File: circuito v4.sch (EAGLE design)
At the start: 64 parts, among them IC1 LM324N

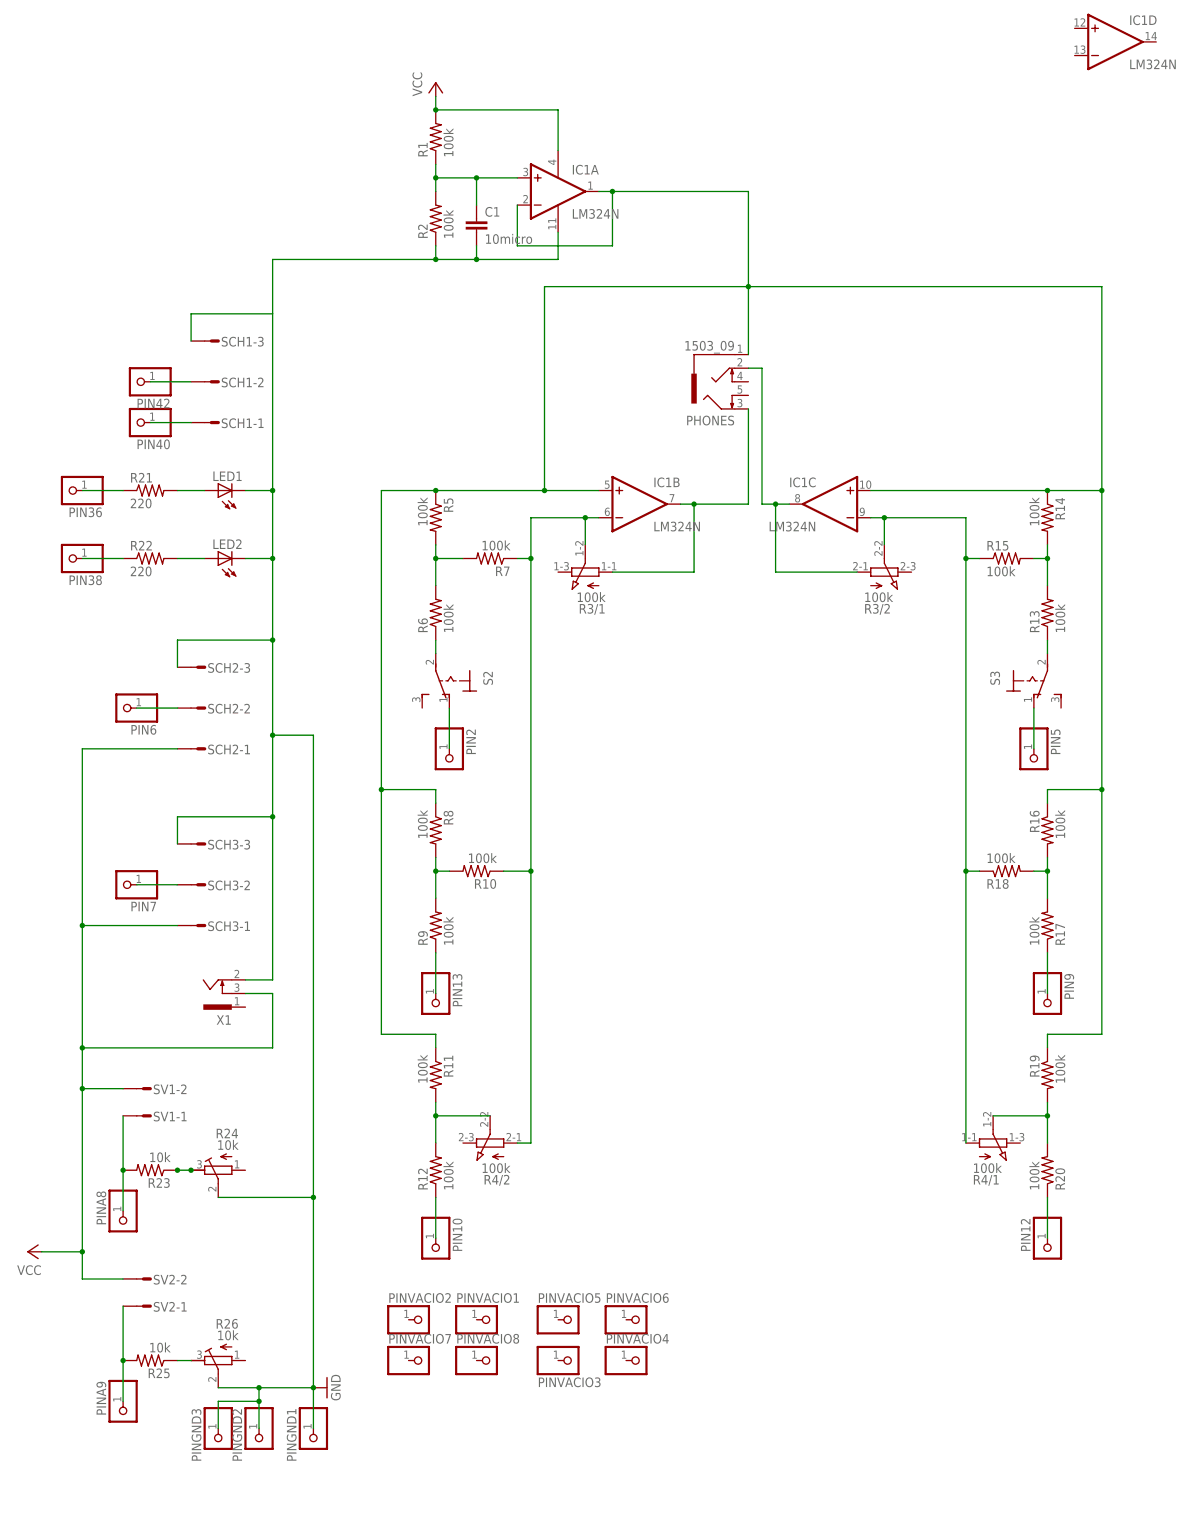
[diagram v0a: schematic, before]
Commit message: Agregado de recuadros con texto
Muestran que es cada parte delcircuito
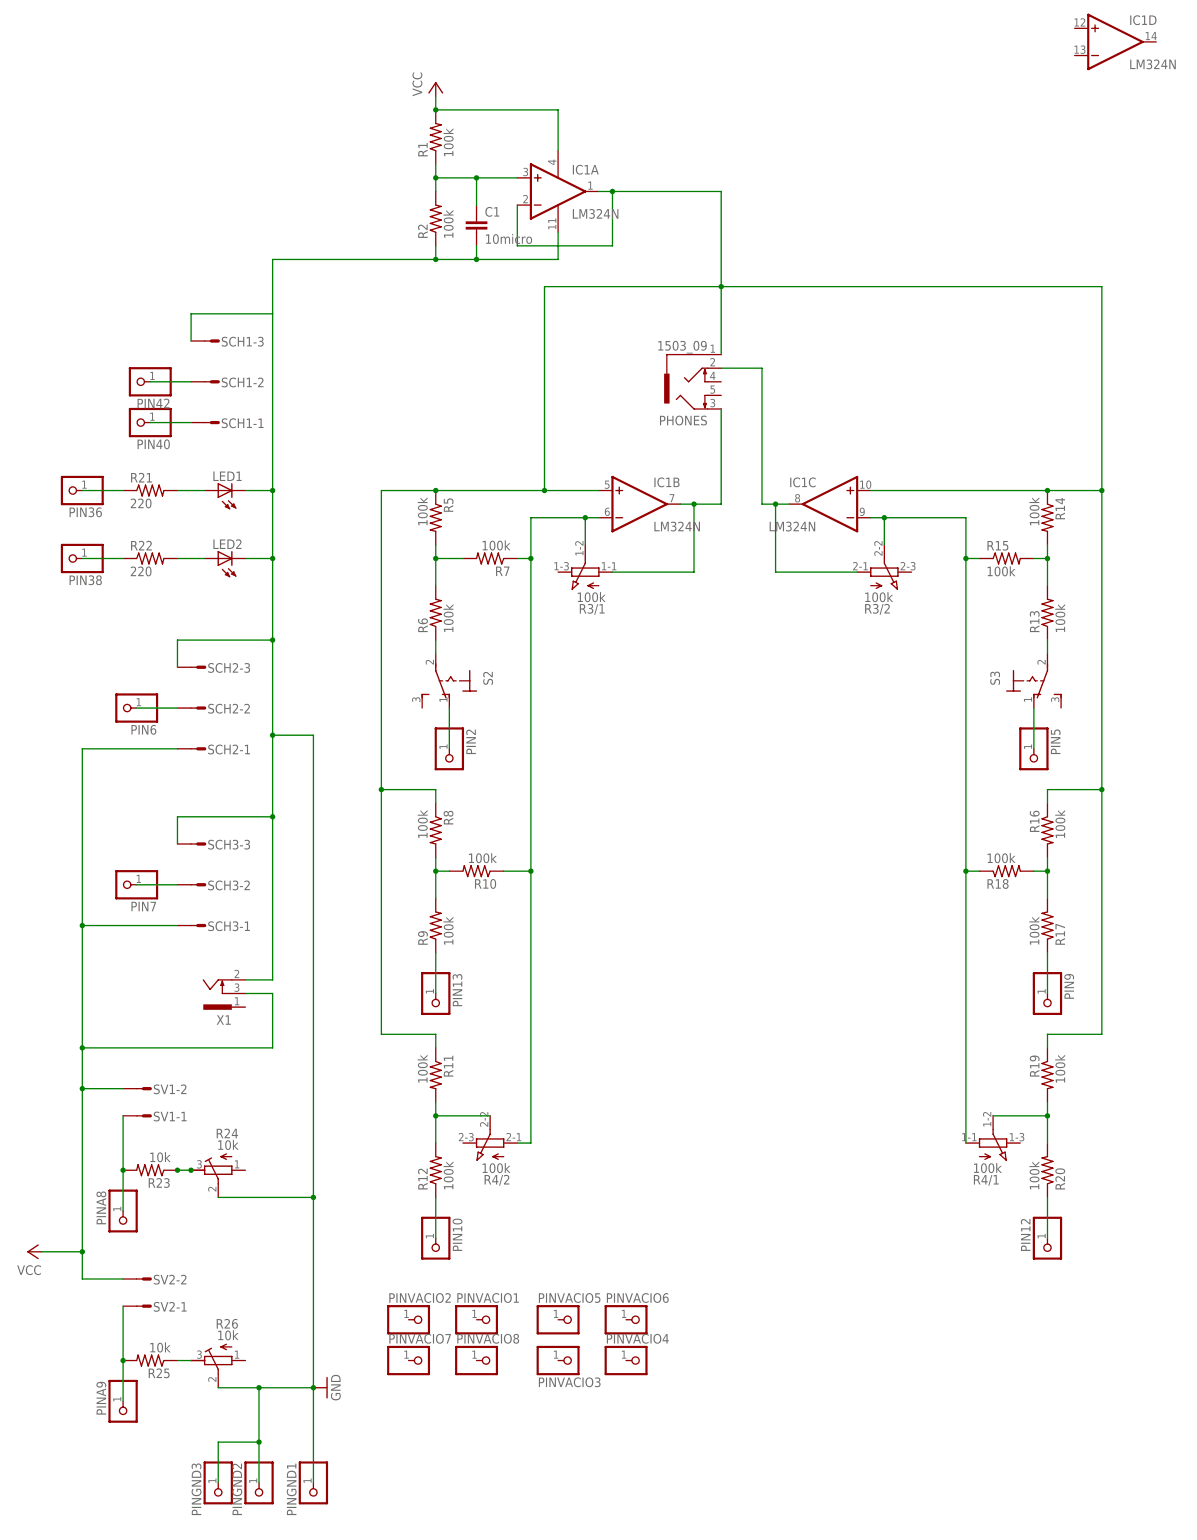
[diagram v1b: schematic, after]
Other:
- note added: "Conexion Servos"
- note added: "FSR (izq y der)"
- note added: "LEDs y sincronizacion"
- note added: "Rama derecha de audio"
- note added: "Rama izquierda del audio"
- note added: "Tierra virtual"
- moved on the sheet: PHONES, PINGND1, PINGND2, PINGND3
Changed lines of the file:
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@@
 <sheet>
 <plain>
+<wire x1="-27.94" y1="106.68" x2="-27.94" y2="63.5" width="0.1524" layer="150"/>
+<wire x1="-27.94" y1="63.5" x2="22.86" y2="63.5" width="0.1524" layer="150"/>
+<wire x1="22.86" y1="63.5" x2="22.86" y2="106.68" width="0.1524" layer="150"/>
+<wire x1="22.86" y1="106.68" x2="-27.94" y2="106.68" width="0.1524" layer="150"/>
+<text x="-10.16" y="109.22" size="1.778" layer="150">Tierra virtual</text>
+<wire x1="-30.48" y1="30.48" x2="35.56" y2="30.48" width="0.1524" layer="150"/>
+<wire x1="35.56" y1="30.48" x2="35.56" y2="-121.92" width="0.1524" layer="150"/>
+<wire x1="35.56" y1="-121.92" x2="-30.48" y2="-121.92" width="0.1524" layer="150"/>
+<wire x1="-30.48" y1="-121.92" x2="-30.48" y2="30.48" width="0.1524" layer="150"/>
+<text x="-22.86" y="33.02" size="1.778" layer="150">Rama derecha de audio</text>
+<wire x1="43.18" y1="30.48" x2="43.18" y2="-121.92" width="0.1524" layer="150"/>
+<wire x1="43.18" y1="-121.92" x2="114.3" y2="-121.92" width="0.1524" layer="150"/>
+<wire x1="114.3" y1="-121.92" x2="114.3" y2="30.48" width="0.1524" layer="150"/>
+<wire x1="114.3" y1="30.48" x2="43.18" y2="30.48" width="0.1524" layer="150"/>
+<text x="73.66" y="33.02" size="1.778" layer="150">Rama izquierda del audio</text>
+<wire x1="-91.44" y1="60.96" x2="-91.44" y2="2.54" width="0.1524" layer="150"/>
+<wire x1="-91.44" y1="2.54" x2="-40.64" y2="2.54" width="0.1524" layer="150"/>
+<wire x1="-40.64" y1="2.54" x2="-40.64" y2="60.96" width="0.1524" layer="150"/>
+<wire x1="-40.64" y1="60.96" x2="-91.44" y2="60.96" width="0.1524" layer="150"/>
+<text x="-78.74" y="63.5" size="1.778" layer="150">LEDs y sincronizacion</text>
+<wire x1="-40.64" y1="-2.54" x2="-91.44" y2="-2.54" width="0.1524" layer="150"/>
+<wire x1="-91.44" y1="-2.54" x2="-91.44" y2="-63.5" width="0.1524" layer="150"/>
+<wire x1="-91.44" y1="-63.5" x2="-40.64" y2="-63.5" width="0.1524" layer="150"/>
+<wire x1="-40.64" y1="-2.54" x2="-40.64" y2="-63.5" width="0.1524" layer="150"/>
+<text x="-73.66" y="-2.54" size="1.778" layer="150">Conexion Servos</text>
+<wire x1="-43.18" y1="-86.36" x2="-96.52" y2="-86.36" width="0.1524" layer="150"/>
+<wire x1="-96.52" y1="-86.36" x2="-96.52" y2="-152.4" width="0.1524" layer="150"/>
+<wire x1="-96.52" y1="-152.4" x2="-43.18" y2="-152.4" width="0.1524" layer="150"/>
+<wire x1="-43.18" y1="-152.4" x2="-43.18" y2="-86.36" width="0.1524" layer="150"/>
+<text x="-76.2" y="-86.36" size="1.778" layer="150">FSR (izq y der)</text>
 </plain>
 <instances>
@@
 <attribute name="VALUE" x="104.14" y="-113.03" size="1.778" layer="96" rot="MR270"/>
 </instance>
-<instance part="PHONES" gate="G$1" x="38.1" y="43.18" smashed="yes" rot="R180">
-<attribute name="NAME" x="40.64" y="36.83" size="1.778" layer="95" rot="R180"/>
-<attribute name="VALUE" x="40.64" y="50.8" size="1.778" layer="96" rot="R180"/>
+<instance part="PHONES" gate="G$1" x="33.02" y="43.18" smashed="yes" rot="R180">
+<attribute name="NAME" x="35.56" y="36.83" size="1.778" layer="95" rot="R180"/>
+<attribute name="VALUE" x="35.56" y="50.8" size="1.778" layer="96" rot="R180"/>
 </instance>
 <instance part="SCH1" gate="-1" x="-55.88" y="35.56" smashed="yes" rot="R180">
@@
 <attribute name="VALUE" x="-88.9" y="-121.92" size="1.778" layer="96" rot="R180"/>
 </instance>
-<instance part="PINGND1" gate="G$1" x="-38.1" y="-154.94" smashed="yes" rot="MR270">
-<attribute name="NAME" x="-41.275" y="-148.59" size="1.778" layer="95" rot="MR270"/>
-<attribute name="VALUE" x="-33.02" y="-148.59" size="1.778" layer="96" rot="MR270"/>
+<instance part="PINGND1" gate="G$1" x="-38.1" y="-165.1" smashed="yes" rot="MR270">
+<attribute name="NAME" x="-41.275" y="-158.75" size="1.778" layer="95" rot="MR270"/>
+<attribute name="VALUE" x="-33.02" y="-158.75" size="1.778" layer="96" rot="MR270"/>
 </instance>
 <instance part="GND1" gate="1" x="-35.56" y="-144.78" smashed="yes" rot="MR270">
 <attribute name="VALUE" x="-33.02" y="-142.24" size="1.778" layer="96" rot="MR270"/>
 </instance>
-<instance part="PINGND2" gate="G$1" x="-48.26" y="-154.94" smashed="yes" rot="MR270">
-<attribute name="NAME" x="-51.435" y="-148.59" size="1.778" layer="95" rot="MR270"/>
-<attribute name="VALUE" x="-43.18" y="-148.59" size="1.778" layer="96" rot="MR270"/>
-</instance>
-<instance part="PINGND3" gate="G$1" x="-55.88" y="-154.94" smashed="yes" rot="MR270">
-<attribute name="NAME" x="-59.055" y="-148.59" size="1.778" layer="95" rot="MR270"/>
-<attribute name="VALUE" x="-50.8" y="-148.59" size="1.778" layer="96" rot="MR270"/>
+<instance part="PINGND2" gate="G$1" x="-48.26" y="-165.1" smashed="yes" rot="MR270">
+<attribute name="NAME" x="-51.435" y="-158.75" size="1.778" layer="95" rot="MR270"/>
+<attribute name="VALUE" x="-43.18" y="-158.75" size="1.778" layer="96" rot="MR270"/>
+</instance>
+<instance part="PINGND3" gate="G$1" x="-55.88" y="-165.1" smashed="yes" rot="MR270">
+<attribute name="NAME" x="-59.055" y="-158.75" size="1.778" layer="95" rot="MR270"/>
+<attribute name="VALUE" x="-50.8" y="-158.75" size="1.778" layer="96" rot="MR270"/>
 </instance>
 <instance part="PINVACIO3" gate="G$1" x="10.16" y="-139.7" smashed="yes" rot="MR180">
@@
 <pinref part="PINGND1" gate="G$1" pin="1"/>
 <wire x1="-38.1" y1="-109.22" x2="-38.1" y2="-22.86" width="0.1524" layer="91"/>
-<wire x1="-38.1" y1="-144.78" x2="-38.1" y2="-152.4" width="0.1524" layer="91"/>
+<wire x1="-38.1" y1="-144.78" x2="-38.1" y2="-162.56" width="0.1524" layer="91"/>
 <pinref part="GND1" gate="1" pin="GND"/>
 <pinref part="PINGND3" gate="G$1" pin="1"/>
-<wire x1="-55.88" y1="-152.4" x2="-55.88" y2="-147.32" width="0.1524" layer="91"/>
-<wire x1="-55.88" y1="-147.32" x2="-48.26" y2="-147.32" width="0.1524" layer="91"/>
-<wire x1="-48.26" y1="-147.32" x2="-48.26" y2="-144.78" width="0.1524" layer="91"/>
+<wire x1="-55.88" y1="-162.56" x2="-55.88" y2="-154.94" width="0.1524" layer="91"/>
+<wire x1="-55.88" y1="-154.94" x2="-48.26" y2="-154.94" width="0.1524" layer="91"/>
+<wire x1="-48.26" y1="-154.94" x2="-48.26" y2="-144.78" width="0.1524" layer="91"/>
 <pinref part="PINGND2" gate="G$1" pin="1"/>
-<wire x1="-48.26" y1="-147.32" x2="-48.26" y2="-152.4" width="0.1524" layer="91"/>
+<wire x1="-48.26" y1="-154.94" x2="-48.26" y2="-162.56" width="0.1524" layer="91"/>
 <junction x="-48.26" y="-144.78"/>
-<junction x="-48.26" y="-147.32"/>
+<junction x="-48.26" y="-154.94"/>
 <pinref part="IC1" gate="P" pin="V-"/>
 <wire x1="7.62" y1="71.12" x2="7.62" y2="66.04" width="0.1524" layer="91"/>
@@
 <segment>
 <pinref part="PHONES" gate="G$1" pin="2"/>
-<wire x1="43.18" y1="45.72" x2="45.72" y2="45.72" width="0.1524" layer="91"/>
+<wire x1="38.1" y1="45.72" x2="45.72" y2="45.72" width="0.1524" layer="91"/>
 <wire x1="45.72" y1="45.72" x2="45.72" y2="20.32" width="0.1524" layer="91"/>
 <wire x1="48.26" y1="20.32" x2="50.8" y2="20.32" width="0.1524" layer="91"/>
@@
 <segment>
 <pinref part="PHONES" gate="G$1" pin="3"/>
-<wire x1="43.18" y1="38.1" x2="43.18" y2="20.32" width="0.1524" layer="91"/>
+<wire x1="38.1" y1="38.1" x2="38.1" y2="20.32" width="0.1524" layer="91"/>
 <pinref part="R3" gate="/1" pin="A"/>
 <pinref part="IC1" gate="B" pin="OUT"/>
@@
 <wire x1="33.02" y1="20.32" x2="33.02" y2="7.62" width="0.1524" layer="91"/>
 <wire x1="33.02" y1="7.62" x2="17.78" y2="7.62" width="0.1524" layer="91"/>
-<wire x1="43.18" y1="20.32" x2="33.02" y2="20.32" width="0.1524" layer="91"/>
+<wire x1="38.1" y1="20.32" x2="33.02" y2="20.32" width="0.1524" layer="91"/>
 <junction x="33.02" y="20.32"/>
 </segment>
@@
 <wire x1="15.24" y1="78.74" x2="17.78" y2="78.74" width="0.1524" layer="91"/>
 <pinref part="IC1" gate="A" pin="-IN"/>
-<wire x1="17.78" y1="78.74" x2="43.18" y2="78.74" width="0.1524" layer="91"/>
+<wire x1="17.78" y1="78.74" x2="38.1" y2="78.74" width="0.1524" layer="91"/>
 <wire x1="0" y1="76.2" x2="0" y2="68.58" width="0.1524" layer="91"/>
 <wire x1="0" y1="68.58" x2="17.78" y2="68.58" width="0.1524" layer="91"/>
 <wire x1="17.78" y1="68.58" x2="17.78" y2="78.74" width="0.1524" layer="91"/>
 <junction x="17.78" y="78.74"/>
-<wire x1="43.18" y1="78.74" x2="43.18" y2="60.96" width="0.1524" layer="91"/>
-<wire x1="43.18" y1="60.96" x2="5.08" y2="60.96" width="0.1524" layer="91"/>
+<wire x1="38.1" y1="78.74" x2="38.1" y2="60.96" width="0.1524" layer="91"/>
+<wire x1="38.1" y1="60.96" x2="5.08" y2="60.96" width="0.1524" layer="91"/>
 <wire x1="5.08" y1="60.96" x2="5.08" y2="22.86" width="0.1524" layer="91"/>
 <pinref part="IC1" gate="B" pin="+IN"/>
@@
 <wire x1="-15.24" y1="-78.74" x2="-15.24" y2="-81.28" width="0.1524" layer="91"/>
 <junction x="-25.4" y="-33.02"/>
-<wire x1="43.18" y1="60.96" x2="109.22" y2="60.96" width="0.1524" layer="91"/>
-<junction x="43.18" y="60.96"/>
+<wire x1="38.1" y1="60.96" x2="109.22" y2="60.96" width="0.1524" layer="91"/>
+<junction x="38.1" y="60.96"/>
 <wire x1="109.22" y1="60.96" x2="109.22" y2="22.86" width="0.1524" layer="91"/>
 <pinref part="IC1" gate="C" pin="+IN"/>
@@
 <pinref part="PHONES" gate="G$1" pin="1"/>
 <wire x1="109.22" y1="-33.02" x2="109.22" y2="-78.74" width="0.1524" layer="91"/>
-<wire x1="43.18" y1="48.26" x2="43.18" y2="60.96" width="0.1524" layer="91"/>
+<wire x1="38.1" y1="48.26" x2="38.1" y2="60.96" width="0.1524" layer="91"/>
 <pinref part="R19" gate="G$1" pin="1"/>
 <wire x1="99.06" y1="-78.74" x2="99.06" y2="-81.28" width="0.1524" layer="91"/>

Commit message: board y sch con elemento ICSP del arduino incluido
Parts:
- added JP19: (no value), pinhead:PINHD-2X3
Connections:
- new net 5V_2: JP19.2
- new net CLK: JP19.3
- new net MISO: JP19.1
- new net MOSI: JP19.4
- new net RESET_2: JP19.5
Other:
- note added: "Arduino Due / MEGA pins"
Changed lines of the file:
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@@
 <part name="S2" library="switch" library_urn="urn:adsk.eagle:library:380" deviceset="320-916" device="" package3d_urn="urn:adsk.eagle:package:27678/1"/>
 <part name="S3" library="switch" library_urn="urn:adsk.eagle:library:380" deviceset="320-916" device="" package3d_urn="urn:adsk.eagle:package:27678/1"/>
+<part name="JP19" library="pinhead" deviceset="PINHD-2X3" device=""/>
 </parts>
 <sheets>
@@
 </segment>
 </net>
+</nets>
+</sheet>
+<sheet>
+<plain>
+<text x="-370.84" y="127" size="2.54" layer="97">Arduino Due / MEGA pins</text>
+</plain>
+<instances>
+<instance part="JP19" gate="A" x="-370.84" y="71.12" smashed="yes">
+<attribute name="NAME" x="-377.19" y="76.835" size="1.778" layer="95"/>
+<attribute name="VALUE" x="-377.19" y="63.5" size="1.778" layer="96"/>
+</instance>
+</instances>
+<busses>
+</busses>
+<nets>
+<net name="CLK" class="0">
+<segment>
+<label x="-386.08" y="71.12" size="1.778" layer="91"/>
+<wire x1="-370.84" y1="71.12" x2="-373.38" y2="71.12" width="0.1524" layer="91"/>
+<pinref part="JP19" gate="A" pin="3"/>
+<junction x="-373.38" y="71.12"/>
+<wire x1="-373.38" y1="71.12" x2="-378.46" y2="71.12" width="0.1524" layer="91"/>
+</segment>
+</net>
+<net name="MISO" class="0">
+<segment>
+<label x="-386.08" y="73.66" size="1.778" layer="91"/>
+<wire x1="-370.84" y1="73.66" x2="-373.38" y2="73.66" width="0.1524" layer="91"/>
+<pinref part="JP19" gate="A" pin="1"/>
+<junction x="-373.38" y="73.66"/>
+<wire x1="-373.38" y1="73.66" x2="-378.46" y2="73.66" width="0.1524" layer="91"/>
+</segment>
+</net>
+<net name="MOSI" class="0">
+<segment>
+<wire x1="-368.3" y1="71.12" x2="-365.76" y2="71.12" width="0.1524" layer="91"/>
+<pinref part="JP19" gate="A" pin="4"/>
+<junction x="-365.76" y="71.12"/>
+<wire x1="-365.76" y1="71.12" x2="-360.68" y2="71.12" width="0.1524" layer="91"/>
+<label x="-358.14" y="71.12" size="1.778" layer="95"/>
+</segment>
+</net>
+<net name="RESET_2" class="0">
+<segment>
+<pinref part="JP19" gate="A" pin="5"/>
+<wire x1="-378.46" y1="68.58" x2="-373.38" y2="68.58" width="0.1524" layer="91"/>
+<label x="-386.08" y="68.58" size="1.778" layer="95"/>
+</segment>
+</net>
+<net name="5V_2" class="0">
+<segment>
+<pinref part="JP19" gate="A" pin="2"/>
+<wire x1="-360.68" y1="73.66" x2="-365.76" y2="73.66" width="0.1524" layer="91"/>
+<label x="-358.14" y="73.66" size="1.778" layer="95"/>
+</segment>
+</net>
+<net name="GND_2" class="0">
+<segment>
+<wire x1="-360.68" y1="68.58" x2="-365.76" y2="68.58" width="0.1524" layer="91"/>
+<wire x1="-368.3" y1="68.58" x2="-365.76" y2="68.58" width="0.1524" layer="91"/>
+<label x="-358.14" y="68.58" size="1.778" layer="95"/>
+</segment>
+</net>
